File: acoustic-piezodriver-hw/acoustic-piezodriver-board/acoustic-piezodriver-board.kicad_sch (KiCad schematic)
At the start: 0 parts

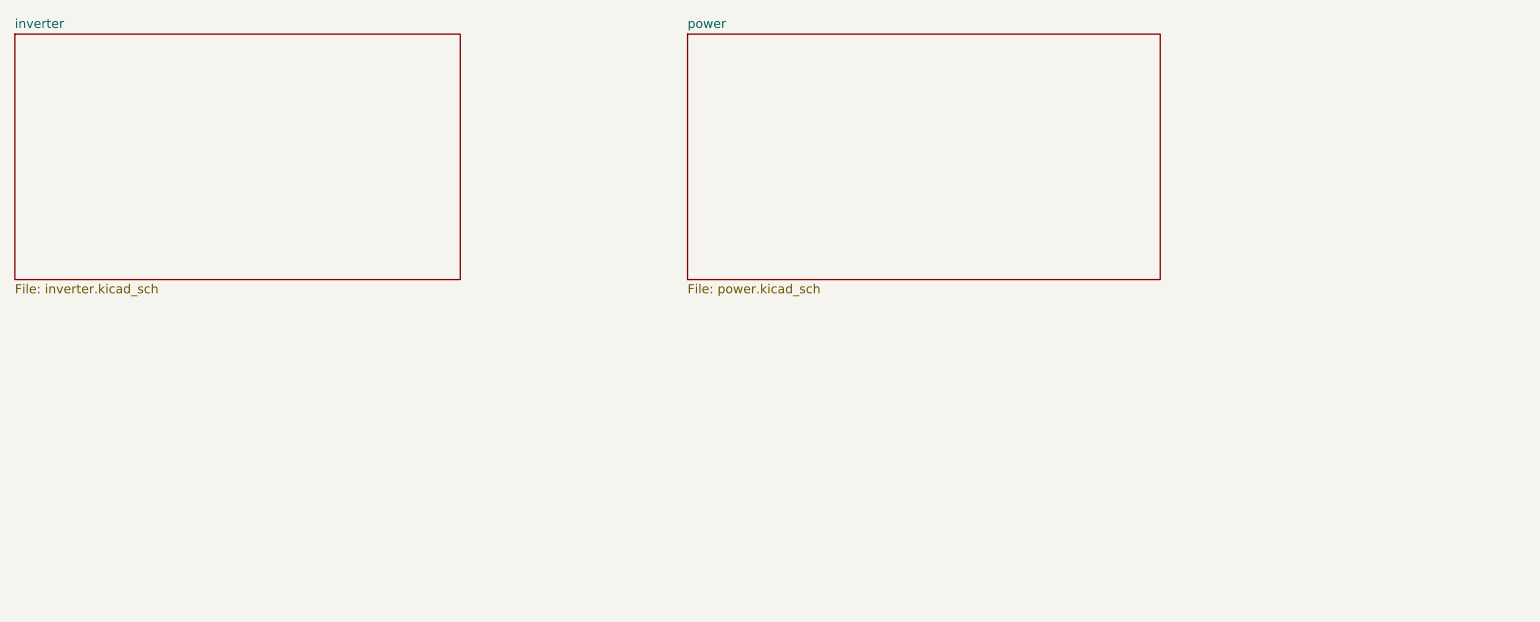
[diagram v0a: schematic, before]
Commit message: [piezodriver] Reorganised piezodriver schematic (next) figure out output filtering
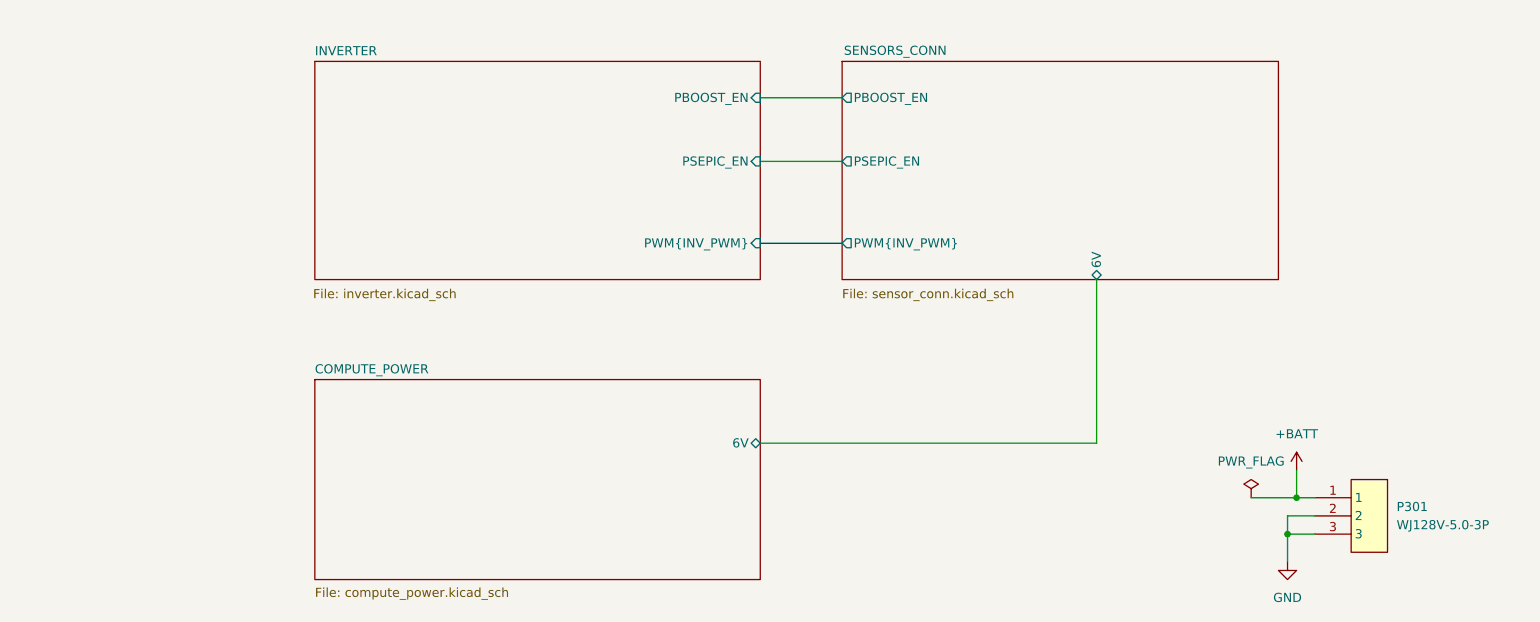
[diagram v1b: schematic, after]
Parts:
- added P301: WJ128V-5.0-3P, iw-connector:WJ128V-5.0-3P, symbol iw-connector:WJ128V-5.0-3P
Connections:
- new net +BATT: P301.1
- new net GND: P301.2, P301.3
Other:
- sheet inverter renamed INVERTER
- sheet power renamed COMPUTE_POWER
- added sheet SENSORS_CONN (sensor_conn.kicad_sch)
- sheet COMPUTE_POWER: file power.kicad_sch -> compute_power.kicad_sch
- sheet COMPUTE_POWER ports: added 6V; removed none
- sheet INVERTER ports: added PBOOST_EN, PSEPIC_EN, PWM{INV_PWM}; removed none
